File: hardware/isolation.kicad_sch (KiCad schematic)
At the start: 16 parts, among them IC2 UCC12040DVER, IC3 MCP1700T-3302E_TT, IC4 ISO7763DBQR, IC5 ISO7741DBQR

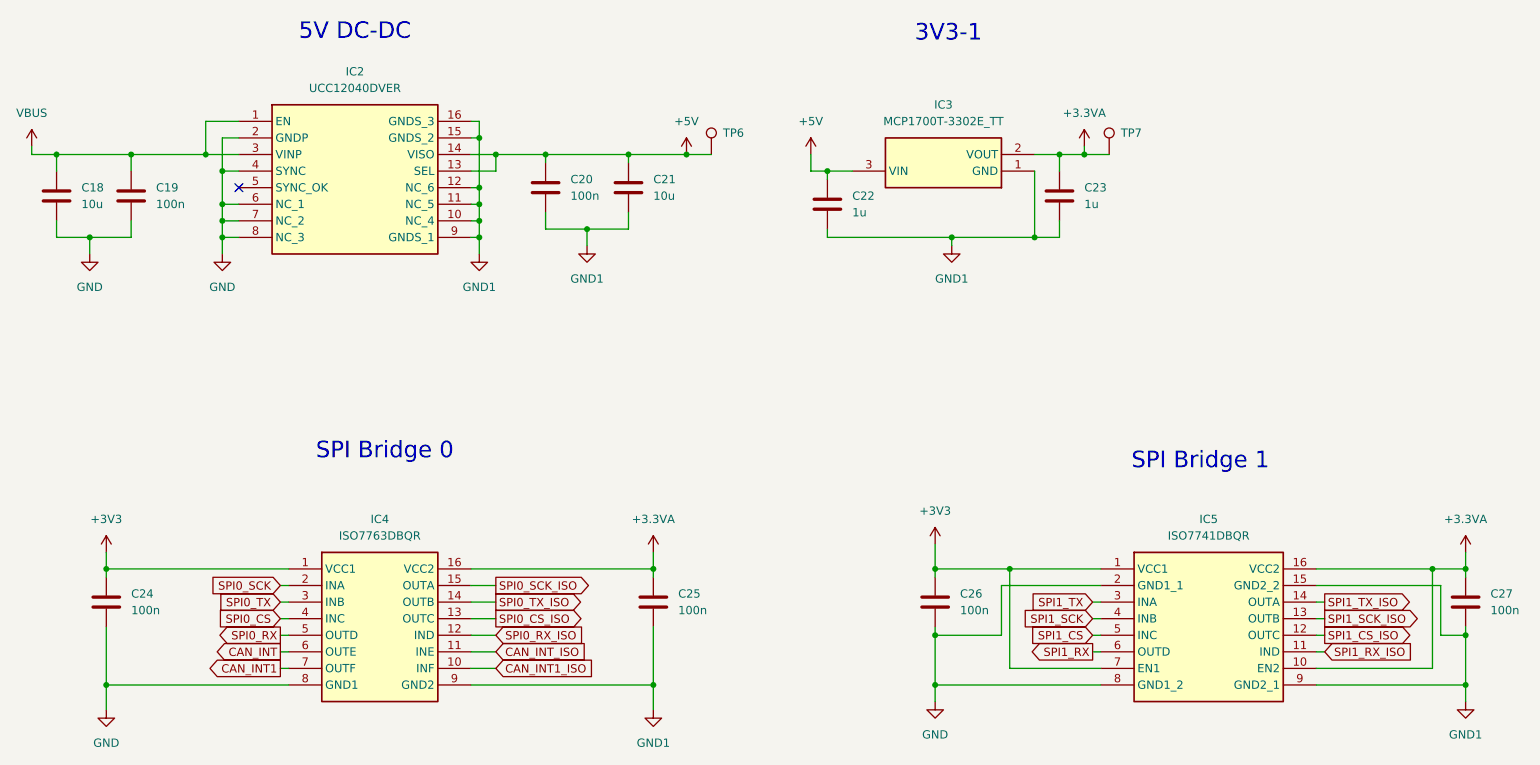
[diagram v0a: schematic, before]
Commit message: Added new DCDC to library
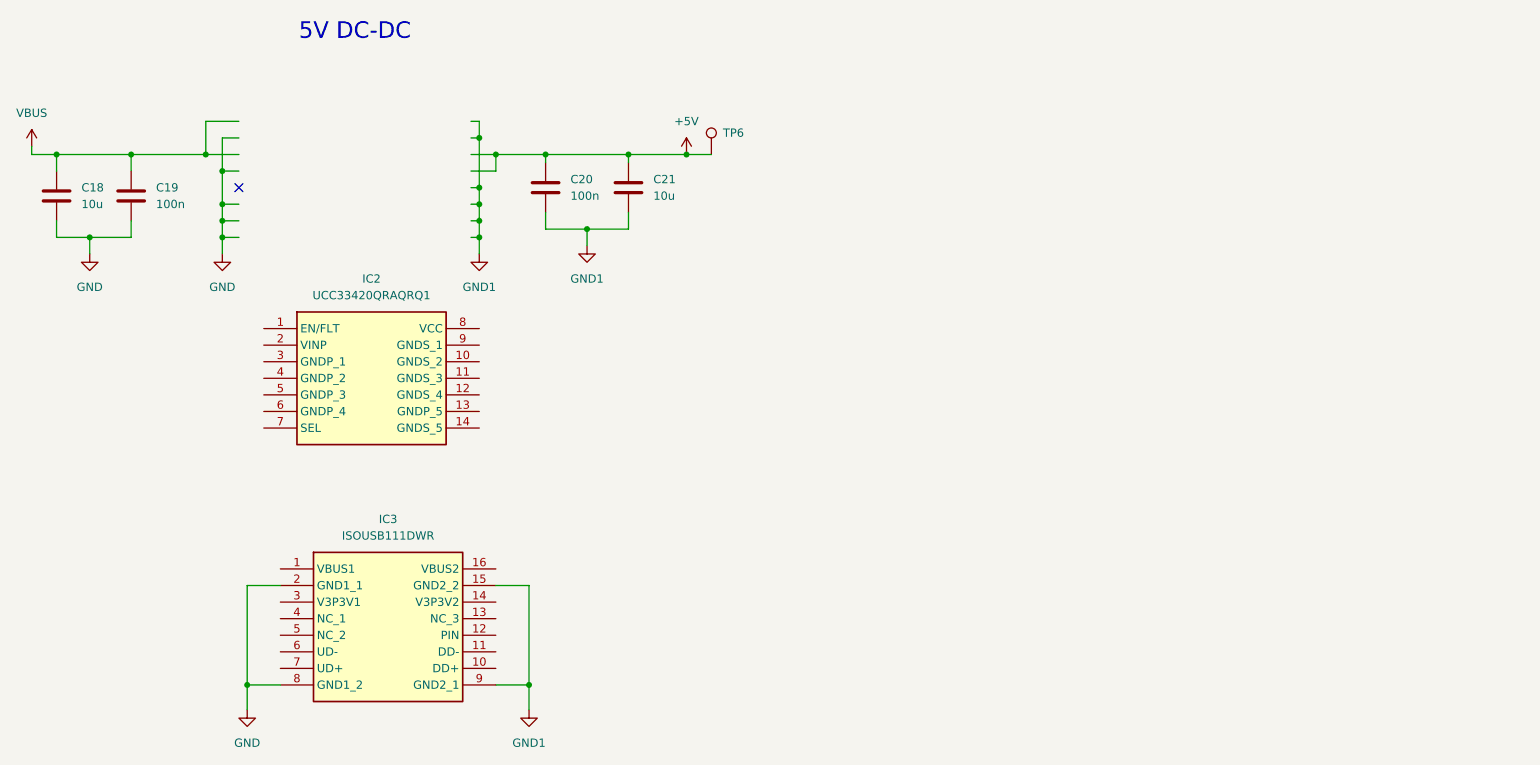
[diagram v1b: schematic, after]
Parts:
- removed C22, C23: 1u, Capacitor_SMD:C_0402_1005Metric, symbol Device:C
- removed C24, C25, C26, C27: 100n, Capacitor_SMD:C_0402_1005Metric, symbol Device:C
- removed IC2: UCC12040DVER, Stuttgart:SOIC127P1030X265-16N, symbol Stuttgart:UCC12040DVER
- removed IC3: MCP1700T-3302E_TT, Stuttgart:SOT95P237X112-3N, symbol Stuttgart:MCP1700T-3302E_TT
- removed IC4: ISO7763DBQR, Stuttgart:SOP64P600X175-16N, symbol Stuttgart:ISO7763DBQR
- removed IC5: ISO7741DBQR, Stuttgart:SOP64P600X175-16N, symbol Stuttgart:ISO7741DBQR
- removed TP7: TestPoint, TestPoint:TestPoint_Pad_D1.0mm, symbol Connector:TestPoint
- added IC2: UCC33420QRAQRQ1, UCC33020QRAQRQ1, symbol Stuttgart:UCC33420QRAQRQ1
- added IC3: ISOUSB111DWR, Stuttgart:SOIC127P1030X265-16N, symbol Stuttgart:ISOUSB111DWR
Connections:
- net GND: now also IC3.2 (GND1_1), IC3.8 (GND1_2)
- net GND1: now also IC3.15 (GND2_2), IC3.9 (GND2_1)
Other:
- note removed: "3V3-1"
- note removed: "SPI Bridge 0"
- note removed: "SPI Bridge 1"
